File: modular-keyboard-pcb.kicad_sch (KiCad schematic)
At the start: 0 parts

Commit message: day 1
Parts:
- added R1, R2: 22, symbol Device:R_Small_US
- added U1: STM32G474RETx, Package_QFP:LQFP-64_10x10mm_P0.5mm, symbol MCU_ST_STM32G4:STM32G474RETx
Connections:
- new net: R2.1, U1.46 (PA12)
- new net: R1.1, U1.45 (PA11)
- new net +3.3V: U1.1 (VBAT), U1.16 (VDD), U1.28 (VREF+), U1.29 (VDDA), U1.32 (VDD), U1.48 (VDD), U1.64 (VDD)
- new net GND: U1.15 (VSS), U1.27 (VSSA), U1.31 (VSS), U1.47 (VSS), U1.63 (VSS)

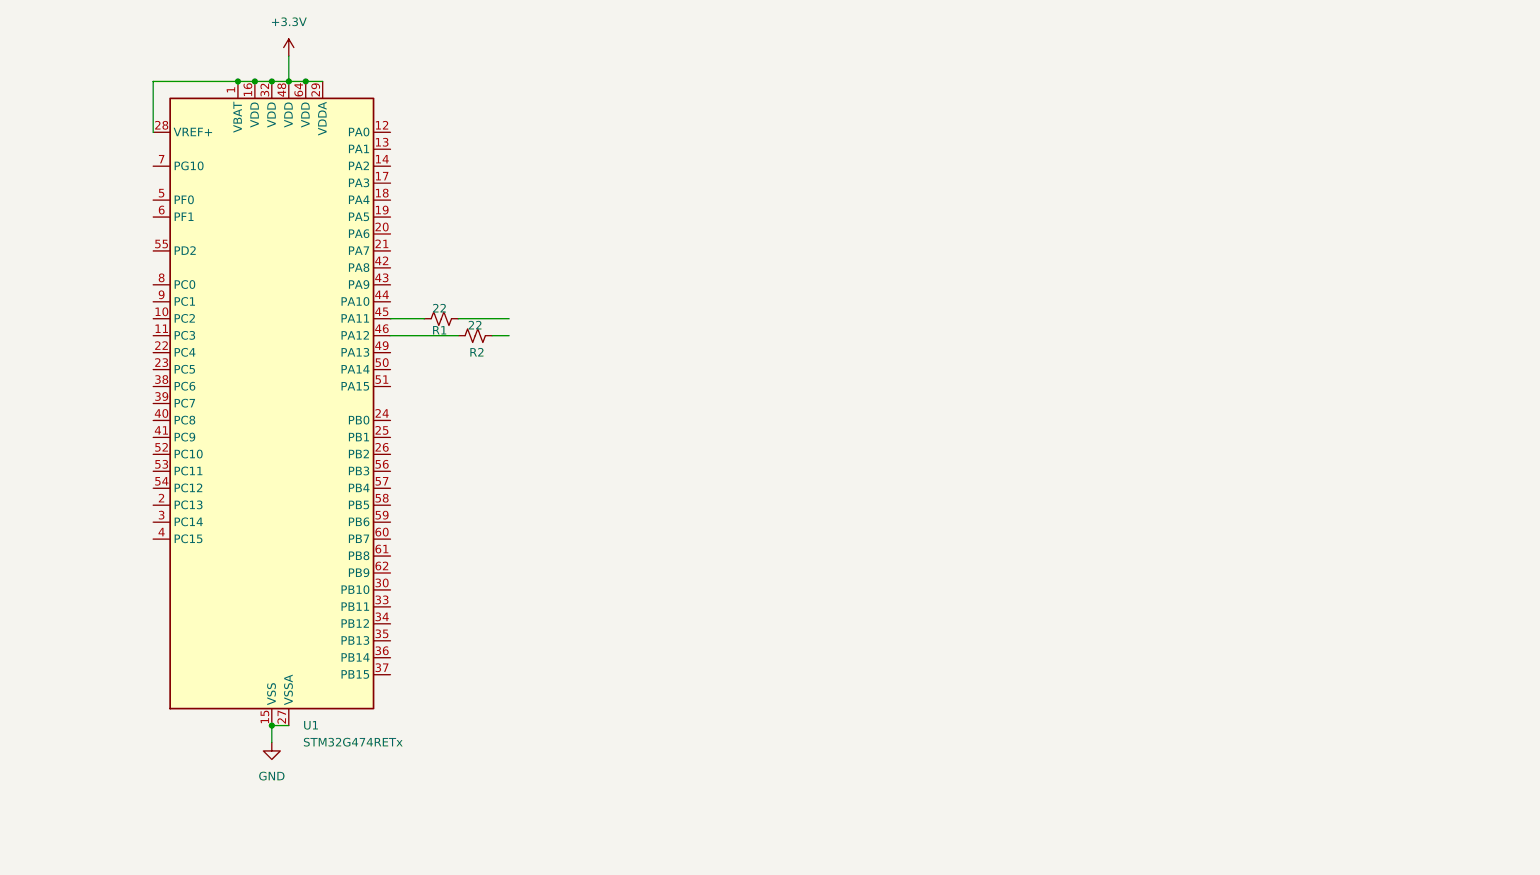
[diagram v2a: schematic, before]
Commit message: day 2
changed to nice nano
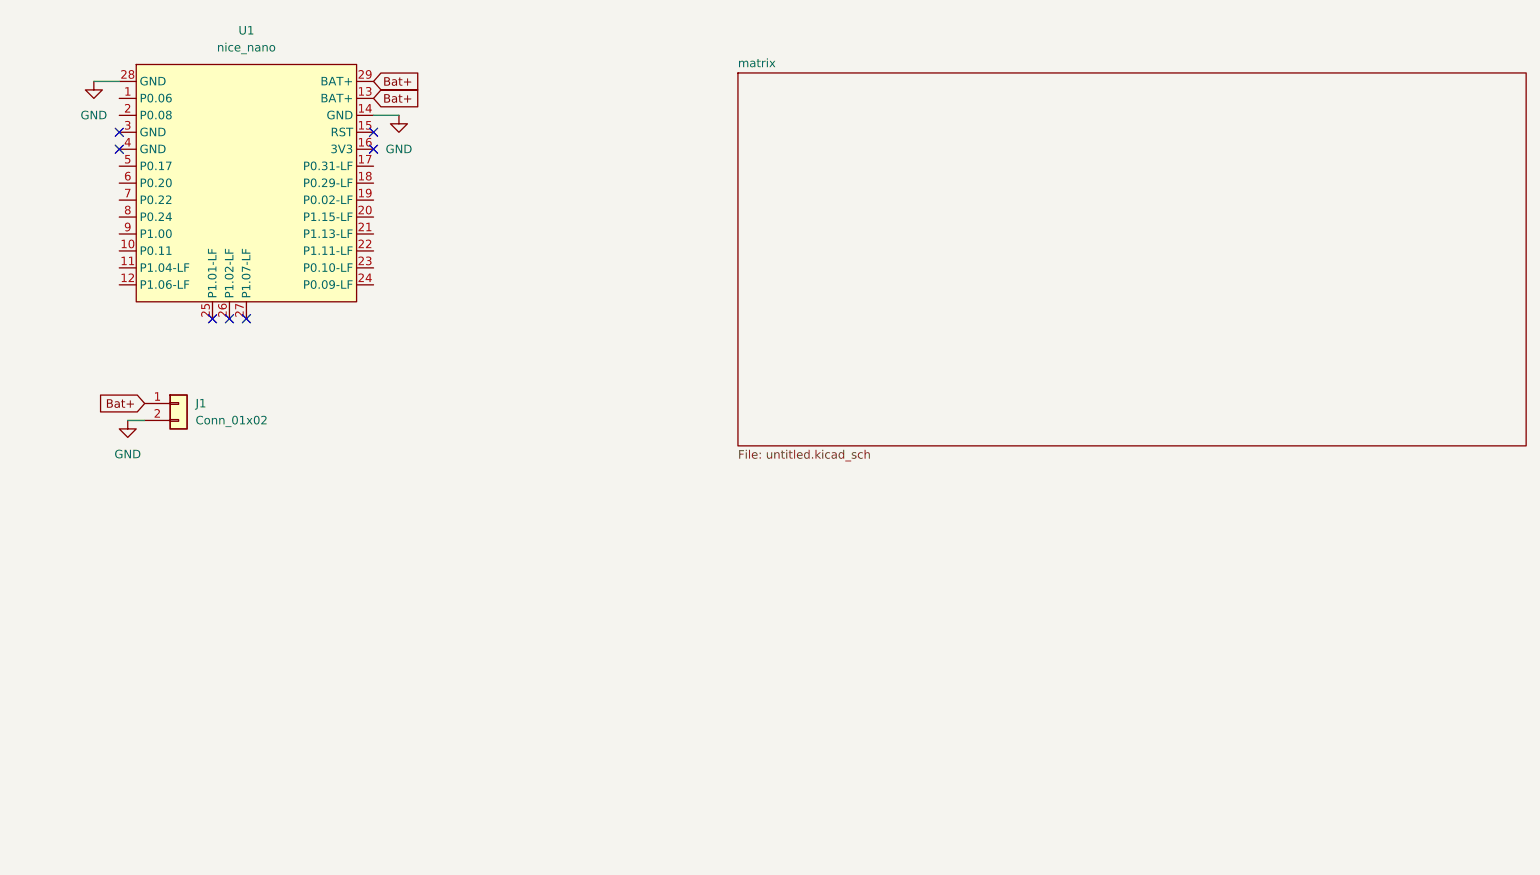
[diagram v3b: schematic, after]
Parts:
- removed R1, R2: 22, symbol Device:R_Small_US
- removed U1: STM32G474RETx, Package_QFP:LQFP-64_10x10mm_P0.5mm, symbol MCU_ST_STM32G4:STM32G474RETx
- added J1: Conn_01x02, symbol Connector_Generic:Conn_01x02
- added U1: nice_nano, PCM_marbastlib-xp-promicroish:nice_nano_AH_USBup, symbol marbastlib-promicroish:nice_nano
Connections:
- net GND: now also J1.2 (Pin_2), U1.14 (GND), U1.28 (GND)
- new net Bat+: J1.1 (Pin_1), U1.13 (BAT+), U1.29 (BAT+)
- no-connect marks 0 -> 7
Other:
- added sheet matrix (untitled.kicad_sch)

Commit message: day 2 end
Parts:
- added J? (x4): mag_pogo_01x05, symbol Connector_Generic:Conn_01x05
- renumbered J1 to J?, U1 to U?
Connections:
- net Bat+: no longer U?.29 (BAT+)
- net GND: now also U?.3 (GND), U?.4 (GND), J?.1 (Pin_1), J?.1 (Pin_1), J?.5 (Pin_5), J?.5 (Pin_5); no longer U?.28 (GND)
- net Col 0: now reaches U?.1 (P0.06)
- net Row 5: now reaches U?.10 (P0.11)
- net Row 5: now also J?.3 (Pin_3), J?.3 (Pin_3)
- net Col 8: now reaches U?.11 (P1.04-LF)
- net Col 8: now also J?.2 (Pin_2), J?.2 (Pin_2)
- net Col 9: now reaches U?.12 (P1.06-LF)
- net Col 9: now also J?.4 (Pin_4), J?.4 (Pin_4)
- net Col 2: now reaches U?.17 (P0.31-LF)
- net Col 3: now reaches U?.18 (P0.29-LF)
- net Col 4: now reaches U?.19 (P0.02-LF)
- net Col 1: now reaches U?.2 (P0.08)
- net Col 5: now reaches U?.20 (P1.15-LF)
- net Col 6: now reaches U?.21 (P1.13-LF)
- net Col 7: now reaches U?.22 (P1.11-LF)
- net Row 0: now reaches U?.5 (P0.17)
- net Row 0: now also J?.3 (Pin_3), J?.3 (Pin_3)
- net Row 1: now reaches U?.6 (P0.20)
- net Row 1: now also J?.4 (Pin_4), J?.4 (Pin_4)
- net Row 2: now reaches U?.7 (P0.22)
- net Row 2: now also J?.5 (Pin_5), J?.5 (Pin_5)
- net Row 3: now reaches U?.8 (P0.24)
- net Row 3: now also J?.1 (Pin_1), J?.1 (Pin_1)
- net Row 4: now reaches U?.9 (P1.00)
- net Row 4: now also J?.2 (Pin_2), J?.2 (Pin_2)
- no-connect marks 7 -> 5

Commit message: day 3 edit 1
schematic finalized
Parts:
- added SW1: SW_Push, symbol Switch:SW_Push
- added SW2: SW_Wuerth_450301014042, Button_Switch_THT:SW_Slide-03_Wuerth-WS-SLTV_10x2.5x6.4_P2.54mm, symbol Switch:SW_Wuerth_450301014042
- J1: renamed from J?; footprint (none) -> Connector_JST:JST_EH_B2B-EH-A_1x02_P2.50mm_Vertical
- J2, J3, J4, J5: renamed from J?; footprint (none) -> Connector_PinHeader_2.54mm:PinHeader_1x05_P2.54mm_Vertical
- gave numbers to parts that had none: 1
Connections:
- net Bat+: now also SW2.2 (C); no longer J1.1 (Pin_1)
- net GND: now also SW1.2, SW2.3 (A)
- net at U1.15 (RST): now also SW1.1
- new net: J1.1 (Pin_1), SW2.1 (B)
- no-connect marks 5 -> 6

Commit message: day 3
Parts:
- SW1: footprint (none) -> SKQG-1155865
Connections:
- net Col 0: now also U1.5 (P0.17); no longer U1.1 (P0.06)
- net Col 1: now also U1.6 (P0.20); no longer U1.2 (P0.08)
- net Col 2: now also U1.7 (P0.22); no longer U1.17 (P0.31-LF)
- net Col 3: now also U1.8 (P0.24); no longer U1.18 (P0.29-LF)
- net Col 4: now also U1.9 (P1.00); no longer U1.19 (P0.02-LF)
- net Col 5: now also U1.10 (P0.11); no longer U1.20 (P1.15-LF)
- net Col 6: now also U1.11 (P1.04-LF); no longer U1.21 (P1.13-LF)
- net Col 7: now also U1.17 (P0.31-LF); no longer U1.22 (P1.11-LF)
- net Col 8: now also U1.18 (P0.29-LF); no longer U1.11 (P1.04-LF)
- net Row 0: now also U1.19 (P0.02-LF); no longer U1.5 (P0.17)
- net Row 1: now also U1.20 (P1.15-LF); no longer U1.6 (P0.20)
- net Row 2: now also U1.21 (P1.13-LF); no longer U1.7 (P0.22)
- net Row 3: now also U1.22 (P1.11-LF); no longer U1.8 (P0.24)
- net Row 4: now also U1.23 (P0.10-LF); no longer U1.9 (P1.00)
- net Row 5: now also U1.24 (P0.09-LF); no longer U1.10 (P0.11)
